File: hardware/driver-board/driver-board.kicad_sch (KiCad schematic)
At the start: 27 parts, among them J1 Conn_ARM_JTAG_SWD_10, J2 USB_C_Receptacle_USB2.0_16P, SW1 SW_Push, U1 STM32F103CBT6, U2 USBLC6-2SC6, Y1 16Mhz

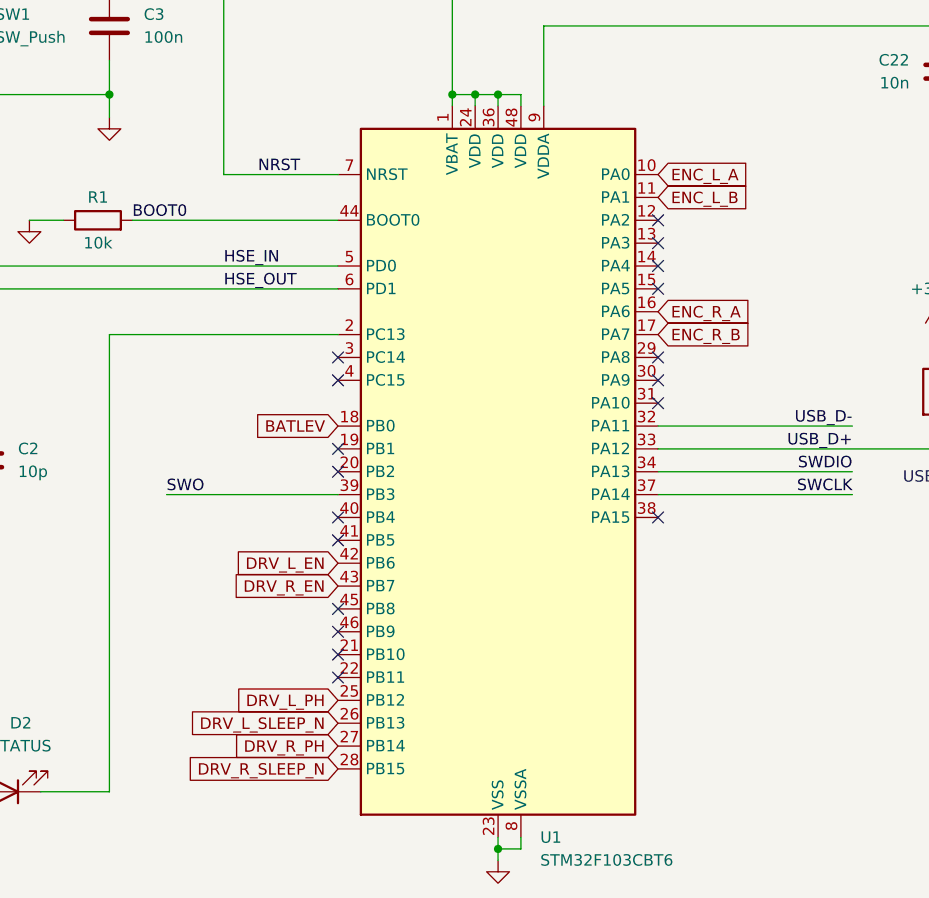
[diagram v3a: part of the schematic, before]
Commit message: Checkpoint left motor driver layout
Capture the routed left motor-driver state before relocation, align the STM32 IOC labels with the schematic pin mapping, and save the current Rev A purchasing and Rev B planning notes.
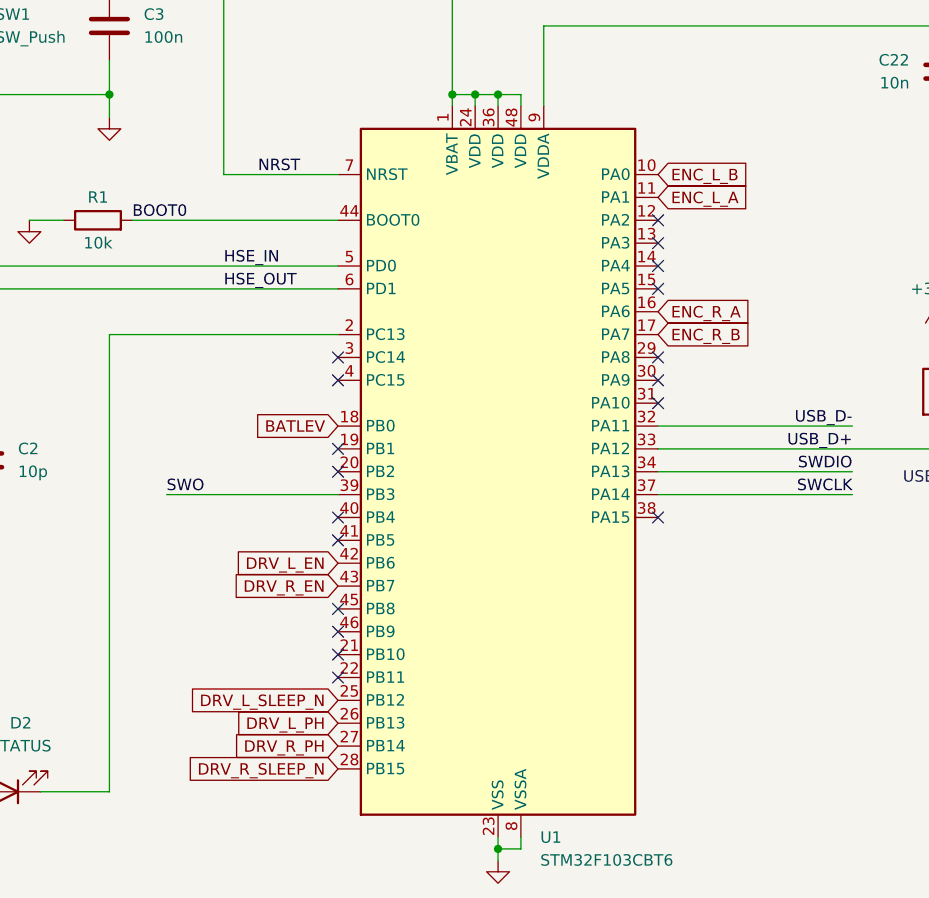
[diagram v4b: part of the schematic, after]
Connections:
- net DRV_L_PH: now also U1.26 (PB13); no longer U1.25 (PB12)
- net DRV_L_SLEEP_N: now also U1.25 (PB12); no longer U1.26 (PB13)
- net ENC_L_A: now also U1.11 (PA1); no longer U1.10 (PA0)
- net ENC_L_B: now also U1.10 (PA0); no longer U1.11 (PA1)
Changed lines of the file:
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@@
 	(global_label "DRV_L_SLEEP_N"
 		(shape input)
+		(at 86.36 120.65 180)
+		(fields_autoplaced yes)
+		(effects
+			(font
+				(size 1.27 1.27)
+			)
+			(justify right)
+		)
+		(property "Intersheetrefs" "${INTERSHEET_REFS}"
+			(at 73.9405 120.65 0)
+			(hide yes)
+			(show_name no)
+			(do_not_autoplace no)
+			(effects
+				(font
+					(size 1.27 1.27)
+				)
+				(justify right)
+			)
+		)
+	)
+	(global_label "DRV_R_EN"
+		(shape input)
+		(at 86.36 107.95 180)
+		(fields_autoplaced yes)
+		(effects
+			(font
+				(size 1.27 1.27)
+			)
+			(justify right)
+		)
+		(property "Intersheetrefs" "${INTERSHEET_REFS}"
+			(at 74.0615 107.95 0)
+			(hide yes)
+			(show_name no)
+			(do_not_autoplace no)
+			(effects
+				(font
+					(size 1.27 1.27)
+				)
+				(justify right)
+			)
+		)
+	)
+	(global_label "DRV_R_SLEEP_N"
+		(shape input)
+		(at 86.36 128.27 180)
+		(fields_autoplaced yes)
+		(effects
+			(font
+				(size 1.27 1.27)
+			)
+			(justify right)
+		)
+		(property "Intersheetrefs" "${INTERSHEET_REFS}"
+			(at 68.4373 128.27 0)
+			(hide yes)
+			(show_name no)
+			(do_not_autoplace no)
+			(effects
+				(font
+					(size 1.27 1.27)
+				)
+				(justify right)
+			)
+		)
+	)
+	(global_label "ENC_R_B"
+		(shape input)
+		(at 121.92 80.01 0)
+		(fields_autoplaced yes)
+		(effects
+			(font
+				(size 1.27 1.27)
+			)
+			(justify left)
+		)
+		(property "Intersheetrefs" "${INTERSHEET_REFS}"
+			(at 133.1299 80.01 0)
+			(hide yes)
+			(show_name no)
+			(do_not_autoplace no)
+			(effects
+				(font
+					(size 1.27 1.27)
+				)
+				(justify left)
+			)
+		)
+	)
+	(global_label "BATLEV"
+		(shape input)
+		(at 86.36 90.17 180)
+		(fields_autoplaced yes)
+		(effects
+			(font
+				(size 1.27 1.27)
+			)
+			(justify right)
+		)
+		(property "Intersheetrefs" "${INTERSHEET_REFS}"
+			(at 76.7829 90.17 0)
+			(hide yes)
+			(show_name no)
+			(do_not_autoplace no)
+			(effects
+				(font
+					(size 1.27 1.27)
+				)
+				(justify right)
+			)
+		)
+	)
+	(global_label "DRV_L_EN"
+		(shape input)
+		(at 86.36 105.41 180)
+		(fields_autoplaced yes)
+		(effects
+			(font
+				(size 1.27 1.27)
+			)
+			(justify right)
+		)
+		(property "Intersheetrefs" "${INTERSHEET_REFS}"
+			(at 74.3034 105.41 0)
+			(hide yes)
+			(show_name no)
+			(do_not_autoplace no)
+			(effects
+				(font
+					(size 1.27 1.27)
+				)
+				(justify right)
+			)
+		)
+	)
+	(global_label "DRV_R_PH"
+		(shape input)
+		(at 86.36 125.73 180)
+		(fields_autoplaced yes)
+		(effects
+			(font
+				(size 1.27 1.27)
+			)
+			(justify right)
+		)
+		(property "Intersheetrefs" "${INTERSHEET_REFS}"
+			(at 68.6792 125.73 0)
+			(hide yes)
+			(show_name no)
+			(do_not_autoplace no)
+			(effects
+				(font
+					(size 1.27 1.27)
+				)
+				(justify right)
+			)
+		)
+	)
+	(global_label "DRV_L_PH"
+		(shape input)
 		(at 86.36 123.19 180)
 		(fields_autoplaced yes)
@@
 		)
 		(property "Intersheetrefs" "${INTERSHEET_REFS}"
-			(at 73.9405 123.19 0)
-			(hide yes)
-			(show_name no)
-			(do_not_autoplace no)
-			(effects
-				(font
-					(size 1.27 1.27)
-				)
-				(justify right)
-			)
-		)
-	)
-	(global_label "DRV_R_EN"
-		(shape input)
-		(at 86.36 107.95 180)
-		(fields_autoplaced yes)
-		(effects
-			(font
-				(size 1.27 1.27)
-			)
-			(justify right)
-		)
-		(property "Intersheetrefs" "${INTERSHEET_REFS}"
-			(at 74.0615 107.95 0)
-			(hide yes)
-			(show_name no)
-			(do_not_autoplace no)
-			(effects
-				(font
-					(size 1.27 1.27)
-				)
-				(justify right)
-			)
-		)
-	)
-	(global_label "DRV_R_SLEEP_N"
-		(shape input)
-		(at 86.36 128.27 180)
-		(fields_autoplaced yes)
-		(effects
-			(font
-				(size 1.27 1.27)
-			)
-			(justify right)
-		)
-		(property "Intersheetrefs" "${INTERSHEET_REFS}"
-			(at 68.4373 128.27 0)
-			(hide yes)
-			(show_name no)
-			(do_not_autoplace no)
-			(effects
-				(font
-					(size 1.27 1.27)
-				)
-				(justify right)
-			)
-		)
-	)
-	(global_label "ENC_R_B"
-		(shape input)
-		(at 121.92 80.01 0)
+			(at 74.1824 123.19 0)
+			(hide yes)
+			(show_name no)
+			(do_not_autoplace no)
+			(effects
+				(font
+					(size 1.27 1.27)
+				)
+				(justify right)
+			)
+		)
+	)
+	(global_label "ENC_L_A"
+		(shape input)
+		(at 121.92 64.77 0)
 		(fields_autoplaced yes)
 		(effects
@@
 		)
 		(property "Intersheetrefs" "${INTERSHEET_REFS}"
-			(at 133.1299 80.01 0)
+			(at 132.7066 64.77 0)
 			(hide yes)
 			(show_name no)
@@
 		)
 	)
-	(global_label "BATLEV"
-		(shape input)
-		(at 86.36 90.17 180)
-		(fields_autoplaced yes)
-		(effects
-			(font
-				(size 1.27 1.27)
-			)
-			(justify right)
-		)
-		(property "Intersheetrefs" "${INTERSHEET_REFS}"
-			(at 76.7829 90.17 0)
-			(hide yes)
-			(show_name no)
-			(do_not_autoplace no)
-			(effects
-				(font
-					(size 1.27 1.27)
-				)
-				(justify right)
-			)
-		)
-	)
-	(global_label "DRV_L_EN"
-		(shape input)
-		(at 86.36 105.41 180)
-		(fields_autoplaced yes)
-		(effects
-			(font
-				(size 1.27 1.27)
-			)
-			(justify right)
-		)
-		(property "Intersheetrefs" "${INTERSHEET_REFS}"
-			(at 74.3034 105.41 0)
-			(hide yes)
-			(show_name no)
-			(do_not_autoplace no)
-			(effects
-				(font
-					(size 1.27 1.27)
-				)
-				(justify right)
-			)
-		)
-	)
-	(global_label "DRV_R_PH"
-		(shape input)
-		(at 86.36 125.73 180)
-		(fields_autoplaced yes)
-		(effects
-			(font
-				(size 1.27 1.27)
-			)
-			(justify right)
-		)
-		(property "Intersheetrefs" "${INTERSHEET_REFS}"
-			(at 68.6792 125.73 0)
-			(hide yes)
-			(show_name no)
-			(do_not_autoplace no)
-			(effects
-				(font
-					(size 1.27 1.27)
-				)
-				(justify right)
-			)
-		)
-	)
-	(global_label "DRV_L_PH"
-		(shape input)
-		(at 86.36 120.65 180)
-		(fields_autoplaced yes)
-		(effects
-			(font
-				(size 1.27 1.27)
-			)
-			(justify right)
-		)
-		(property "Intersheetrefs" "${INTERSHEET_REFS}"
-			(at 74.1824 120.65 0)
-			(hide yes)
-			(show_name no)
-			(do_not_autoplace no)
-			(effects
-				(font
-					(size 1.27 1.27)
-				)
-				(justify right)
-			)
-		)
-	)
-	(global_label "ENC_L_A"
+	(global_label "ENC_L_B"
 		(shape input)
 		(at 121.92 62.23 0)
@@
 		)
 		(property "Intersheetrefs" "${INTERSHEET_REFS}"
-			(at 132.7066 62.23 0)
-			(hide yes)
-			(show_name no)
-			(do_not_autoplace no)
-			(effects
-				(font
-					(size 1.27 1.27)
-				)
-				(justify left)
-			)
-		)
-	)
-	(global_label "ENC_L_B"
-		(shape input)
-		(at 121.92 64.77 0)
-		(fields_autoplaced yes)
-		(effects
-			(font
-				(size 1.27 1.27)
-			)
-			(justify left)
-		)
-		(property "Intersheetrefs" "${INTERSHEET_REFS}"
-			(at 132.888 64.77 0)
-			(hide yes)
-			(show_name no)
+			(at 132.888 62.23 0)
+			(hide yes)
+			(show_name no)

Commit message: Checkpoint left driver and firmware pin mapping
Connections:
- net DRV_L_EN: now also U1.27 (PB14); no longer U1.42 (PB6)
- net DRV_R_PH: now also U1.42 (PB6); no longer U1.27 (PB14)
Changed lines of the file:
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@@
 		)
 	)
-	(global_label "DRV_L_EN"
+	(global_label "DRV_R_PH"
 		(shape input)
 		(at 86.36 105.41 180)
@@
 		)
 	)
-	(global_label "DRV_R_PH"
+	(global_label "DRV_L_EN"
 		(shape input)
 		(at 86.36 125.73 180)

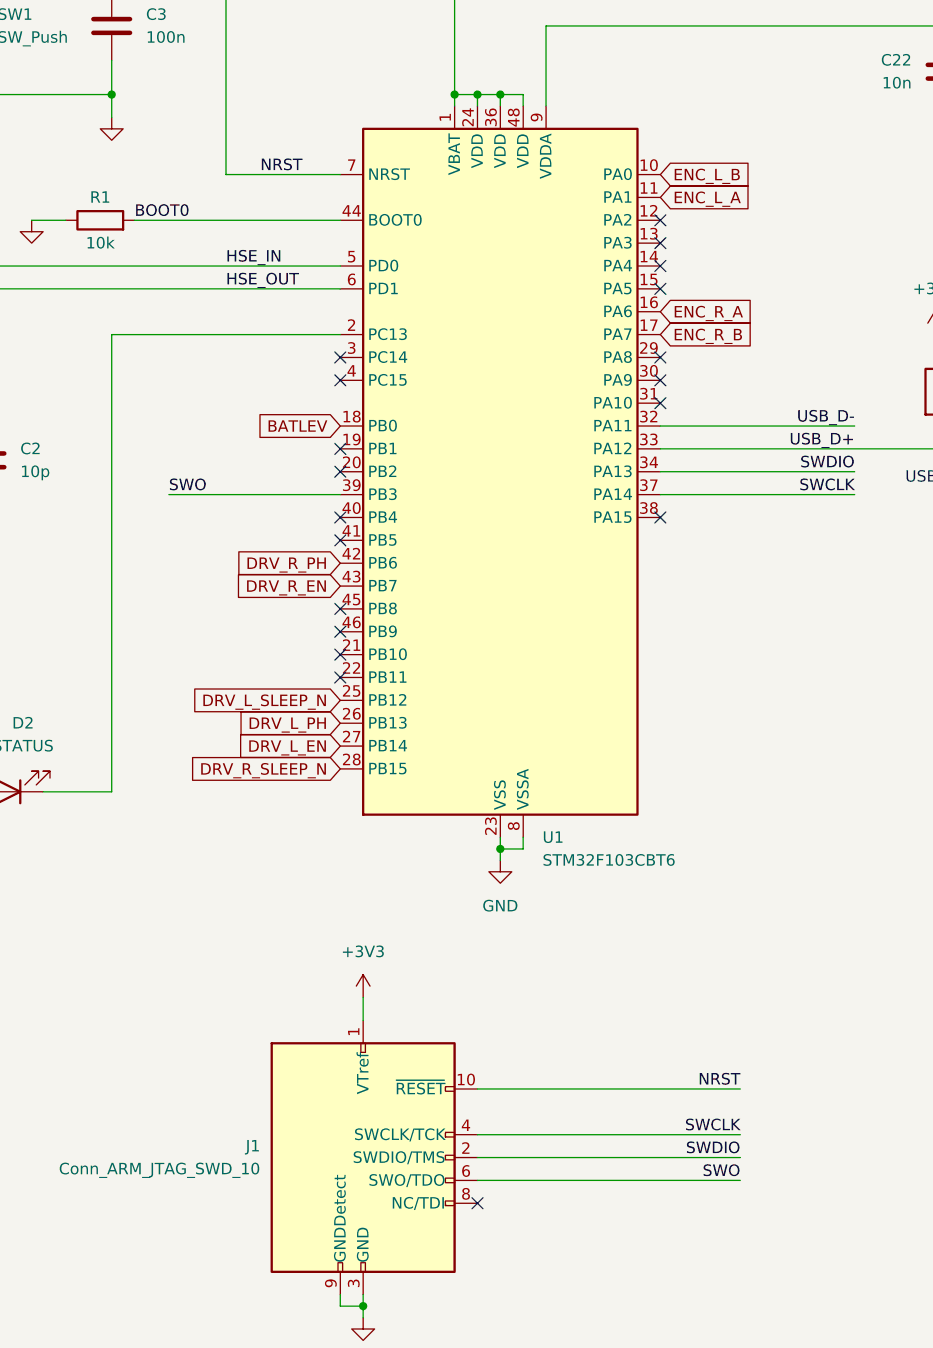
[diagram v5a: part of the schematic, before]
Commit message: Complete motor driver layouts and pin mapping
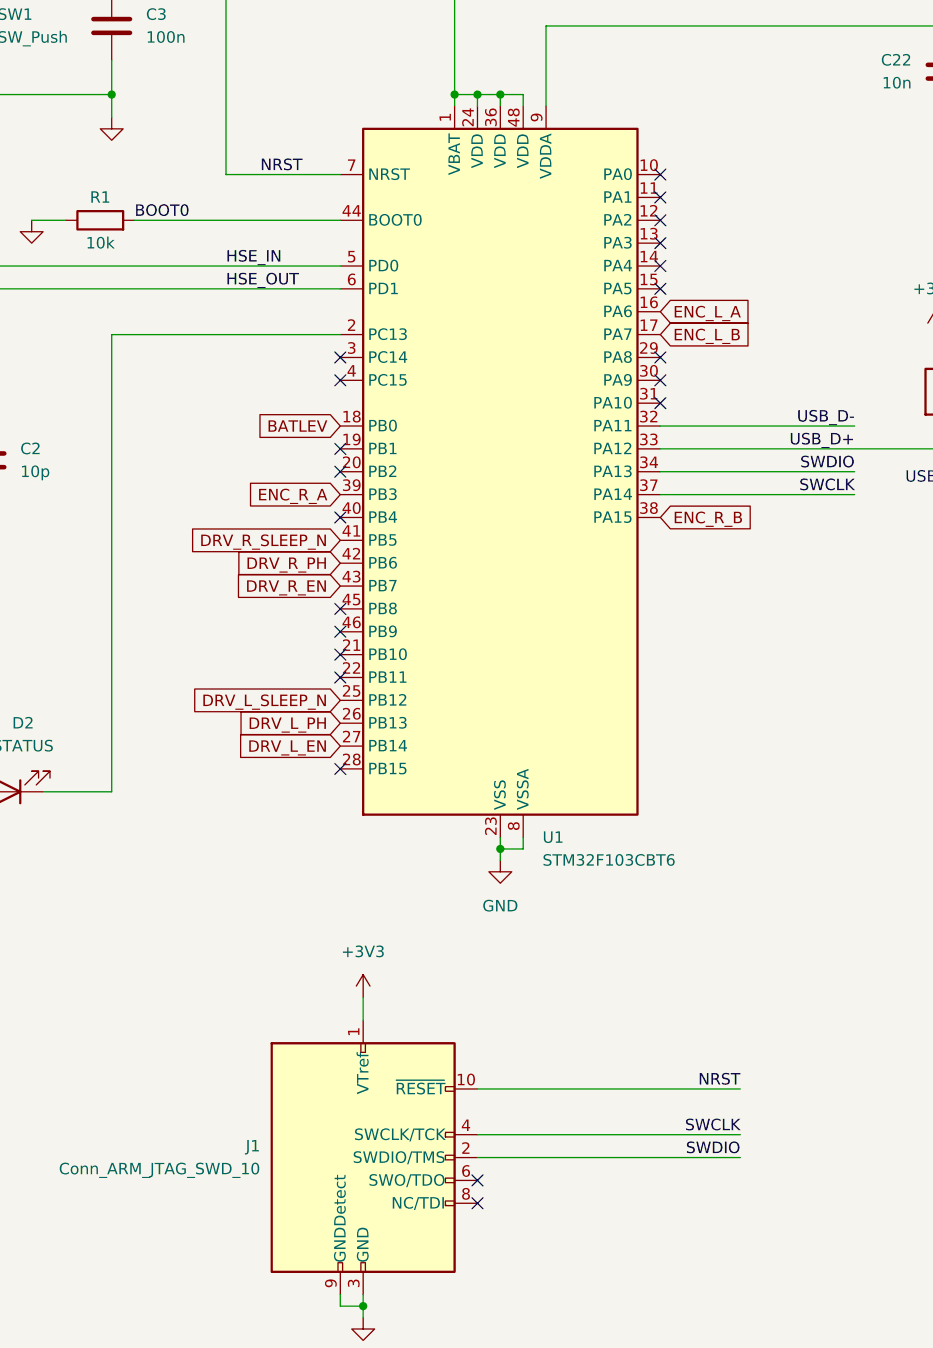
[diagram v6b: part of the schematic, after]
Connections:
- net DRV_R_SLEEP_N: now also U1.41 (PB5); no longer U1.28 (PB15)
- net ENC_L_A: now also U1.16 (PA6); no longer U1.11 (PA1)
- net ENC_L_B: now also U1.17 (PA7); no longer U1.10 (PA0)
- net ENC_R_A: now also U1.39 (PB3); no longer U1.16 (PA6)
- net ENC_R_B: now also U1.38 (PA15); no longer U1.17 (PA7)
- net SWO: no longer names the net of J1.6 (SWO/TDO)
- net SWO: no longer U1.39 (PB3)
- no-connect marks 21 -> 23
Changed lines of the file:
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@@
 	)
 	(no_connect
-		(at 121.92 100.33)
+		(at 121.92 62.23)
 	)
 	(no_connect
@@
 	)
 	(no_connect
-		(at 86.36 102.87)
+		(at 86.36 128.27)
 	)
 	(no_connect
@@
 	)
 	(no_connect
+		(at 101.6 173.99)
+	)
+	(no_connect
 		(at 86.36 115.57)
 	)
@@
 	)
 	(no_connect
+		(at 121.92 64.77)
+	)
+	(no_connect
 		(at 86.36 110.49)
 	)
@@
 	(wire
 		(pts
-			(xy 67.31 97.79) (xy 86.36 97.79)
-		)
-		(stroke
-			(width 0)
-			(type default)
-		)
-	)
-	(wire
-		(pts
 			(xy 162.56 33.02) (xy 173.99 33.02)
 		)
@@
 		(pts
 			(xy 104.14 53.34) (xy 101.6 53.34)
-		)
-		(stroke
-			(width 0)
-			(type default)
-		)
-	)
-	(wire
-		(pts
-			(xy 101.6 173.99) (xy 130.81 173.99)
 		)
 		(stroke
@@
 		)
 	)
-	(label "SWO"
-		(at 130.81 173.99 180)
-		(effects
-			(font
-				(size 1.27 1.27)
-			)
-			(justify right bottom)
-		)
-	)
 	(label "SWDIO"
 		(at 143.51 95.25 180)
@@
 	(label "HSE_OUT"
 		(at 73.66 74.93 0)
-		(effects
-			(font
-				(size 1.27 1.27)
-			)
-			(justify left bottom)
-		)
-	)
-	(label "SWO"
-		(at 67.31 97.79 0)
 		(effects
 			(font
@@
 	(global_label "DRV_R_SLEEP_N"
 		(shape input)
-		(at 86.36 128.27 180)
+		(at 86.36 102.87 180)
 		(fields_autoplaced yes)
 		(effects
@@
 		)
 		(property "Intersheetrefs" "${INTERSHEET_REFS}"
-			(at 68.4373 128.27 0)
+			(at 68.4373 102.87 0)
 			(hide yes)
 			(show_name no)
@@
 	(global_label "ENC_R_B"
 		(shape input)
-		(at 121.92 80.01 0)
+		(at 121.92 100.33 0)
 		(fields_autoplaced yes)
 		(effects
@@
 		)
 		(property "Intersheetrefs" "${INTERSHEET_REFS}"
-			(at 133.1299 80.01 0)
+			(at 133.1299 100.33 0)
 			(hide yes)
 			(show_name no)
@@
 	(global_label "ENC_L_A"
 		(shape input)
-		(at 121.92 64.77 0)
+		(at 121.92 77.47 0)
 		(fields_autoplaced yes)
 		(effects
@@
 		)
 		(property "Intersheetrefs" "${INTERSHEET_REFS}"
-			(at 132.7066 64.77 0)
+			(at 132.7066 77.47 0)
 			(hide yes)
 			(show_name no)
@@
 	(global_label "ENC_L_B"
 		(shape input)
-		(at 121.92 62.23 0)
+		(at 121.92 80.01 0)
 		(fields_autoplaced yes)
 		(effects
@@
 		)
 		(property "Intersheetrefs" "${INTERSHEET_REFS}"
-			(at 132.888 62.23 0)
+			(at 132.888 80.01 0)
 			(hide yes)
 			(show_name no)
@@
 	(global_label "ENC_R_A"
 		(shape input)
-		(at 121.92 77.47 0)
+		(at 86.36 97.79 180)
 		(fields_autoplaced yes)
 		(effects
@@
 				(size 1.27 1.27)
 			)
-			(justify left)
+			(justify right)
 		)
 		(property "Intersheetrefs" "${INTERSHEET_REFS}"
-			(at 132.9485 77.47 0)
+			(at 75.3315 97.79 0)
 			(hide yes)
 			(show_name no)
@@
 					(size 1.27 1.27)
 				)
-				(justify left)
-			)
-		)
+				(justify right)
+			)
+		)

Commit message: Checkpoint status LED move to PB4
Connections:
- net at U1.2 (PC13): no longer D2.1 (K)
- net at U1.40 (PB4): now also D2.1 (K)
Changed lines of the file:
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@@
-	)
-	(no_connect
-		(at 86.36 100.33)
 	)
 	(no_connect
@@
 	)
 	(no_connect
+		(at 86.36 80.01)
+	)
+	(no_connect
 		(at 86.36 115.57)
 	)
@@
 	(wire
 		(pts
-			(xy 86.36 80.01) (xy 60.96 80.01)
-		)
-		(stroke
-			(width 0)
-			(type default)
-		)
-	)
-	(wire
-		(pts
 			(xy 173.99 31.75) (xy 173.99 33.02)
 		)
@@
 	(wire
 		(pts
-			(xy 60.96 80.01) (xy 60.96 130.81)
+			(xy 60.96 100.33) (xy 60.96 130.81)
 		)
 		(stroke
@@
 		)
 		(stroke
+			(width 0)
+			(type default)
+		)
+	)
+	(wire
+		(pts
+			(xy 60.96 100.33) (xy 86.36 100.33)
+		)
+		(stroke

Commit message: Finalize Rev A PCB and hardware docs
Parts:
- C22: JLCPCB (none) -> C15195
- C23: JLCPCB (none) -> C15849
- R5: JLCPCB (none) -> C25867
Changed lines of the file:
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@@
 			)
 		)
-		(property "JLCPCB" ""
+		(property "JLCPCB" "C25867"
 			(at 152.4 86.36 0)
 			(hide yes)
@@
 			)
 		)
-		(property "JLCPCB" ""
+		(property "JLCPCB" "C15195"
 			(at 153.67 50.8 0)
 			(hide yes)
@@
 			)
 		)
-		(property "JLCPCB" ""
+		(property "JLCPCB" "C15849"
 			(at 165.1 50.8 0)
 			(hide yes)
